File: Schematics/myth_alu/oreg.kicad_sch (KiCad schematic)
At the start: 7 parts, among them U11 74HC283, U12 74HC283, U13 74HC157, U14 74HC157, U15 74LS32, U16 74AHC273, U17 74AHC244

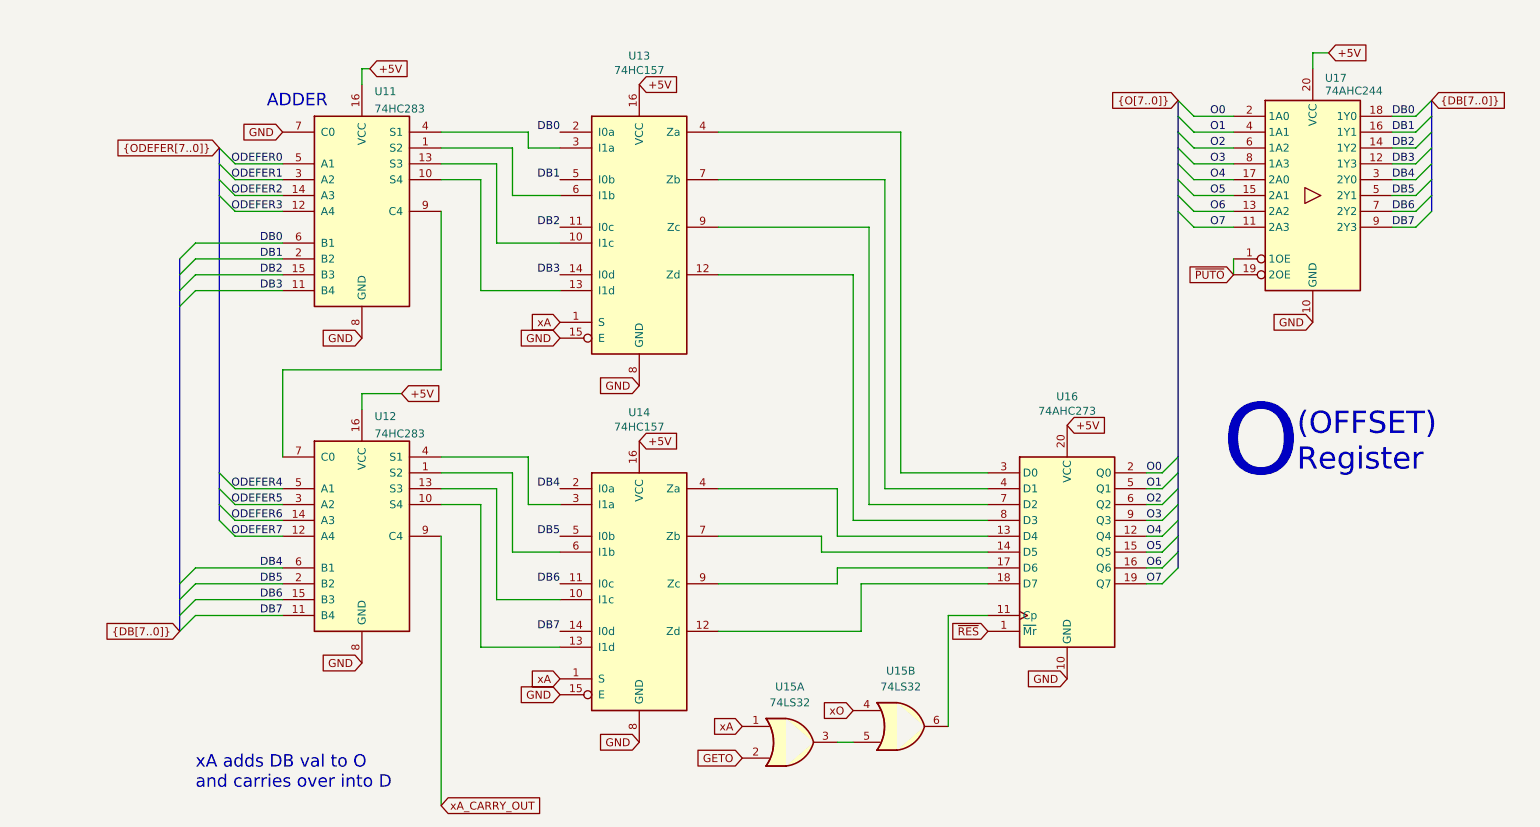
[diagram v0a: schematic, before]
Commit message: Change d to g
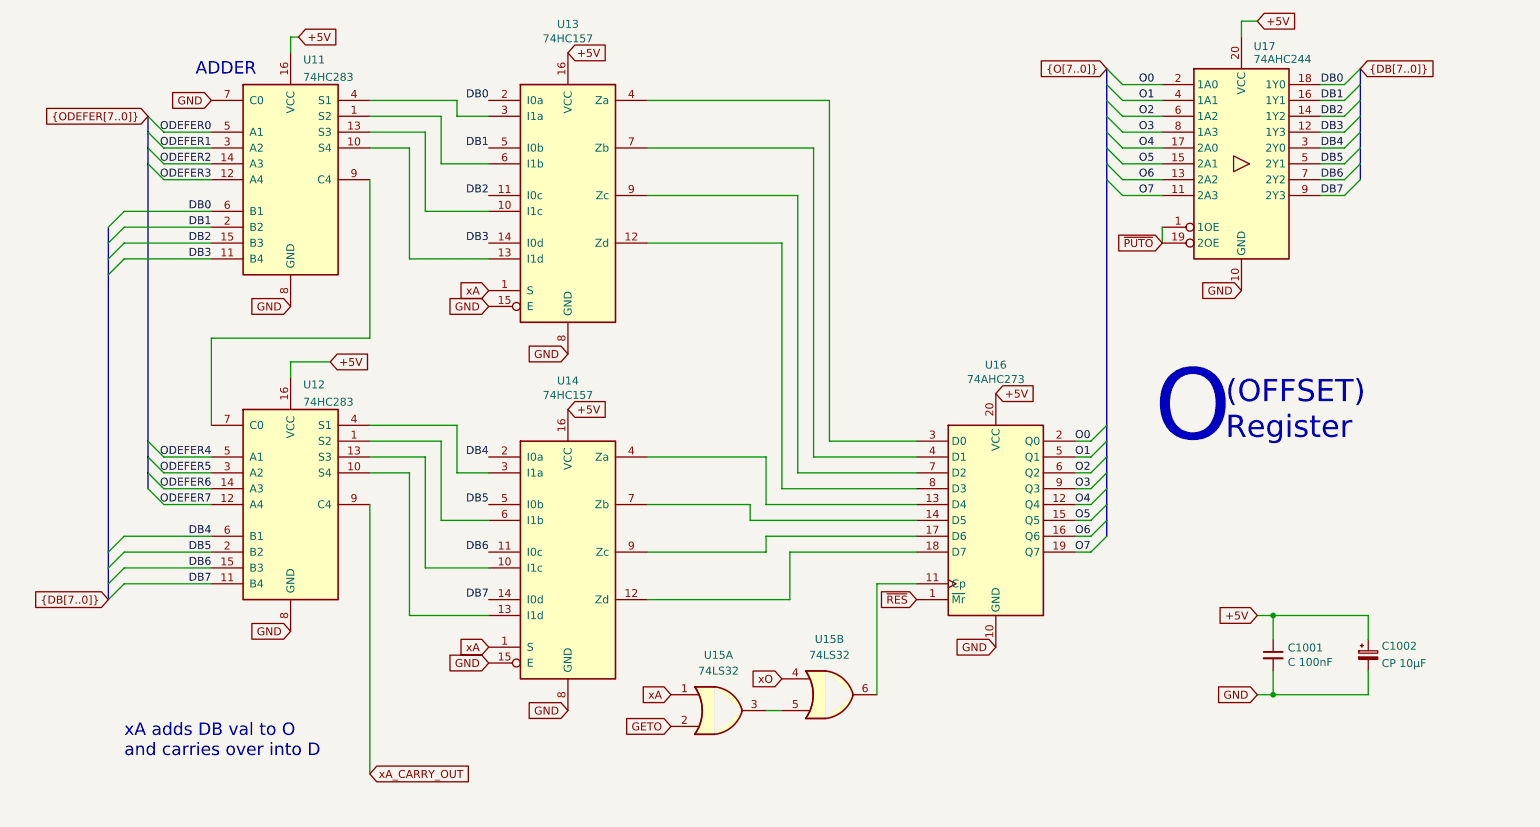
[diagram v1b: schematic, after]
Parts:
- added C1001: C 100nF, Capacitor_THT:C_Disc_D5.0mm_W2.5mm_P2.50mm, symbol Device:C_Small
- added C1002: CP 10μF, Capacitor_THT:CP_Radial_D6.3mm_P2.50mm, symbol Device:C_Polarized_Small
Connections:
- net +5V: now also C1001.1, C1002.1
- net GND: now also C1001.2, C1002.2
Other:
- moved on the sheet: U11, U12, U13, U14, U15A, U15B, U16, U17
